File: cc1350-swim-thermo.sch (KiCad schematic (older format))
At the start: 54 parts, among them P1 LMT_70_1, P2 LMT_70_2, P3 SMA FEMALE, P4 USB_OTG, P5 CONN_02X05, Q1 2N7002, SW1 SW_Push, U1 2450BM14G0011T, U2 XMSSJE3G0PA-003, U3 CC1350F128RSM, U4 TLV713, U5 TLC5973, U6 MCP16251, U7 LFB18868MBG9E212, Y1 24MHz, Y2 32.768kHz

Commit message: checked first iteration of pcb with real components
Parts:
- AE1: footprint cc1350:2450AT42A100 -> cc1350:2450AT45A100
- D1: value CLV1A-FKB -> ASMB-MTB0-0A3A2; footprint LEDs:LED_WS2812B-PLCC4 -> cc1350:ASMB-MTB0-0A3A2
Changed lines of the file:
@@
-$EndComp
-$Comp
-L LED_ARGB D1
-U 1 1 58C766EA
-P 8500 3250
-F 0 "D1" H 8500 3620 50  0000 C CNN
-F 1 "CLV1A-FKB" H 8500 2900 50  0000 C CNN
-F 2 "LEDs:LED_WS2812B-PLCC4" H 8500 3200 50  0001 C CNN
-F 3 "" H 8500 3200 50  0000 C CNN
-	1    8500 3250
-	-1   0    0    1
 $EndComp
 $Comp
@@
 NoConn ~ 7350 5250
 $Comp
-L GND #PWR046
+L GND #PWR045
 U 1 1 58CA0220
 P 7250 5450
-F 0 "#PWR046" H 7250 5200 50  0001 C CNN
+F 0 "#PWR045" H 7250 5200 50  0001 C CNN
 F 1 "GND" H 7250 5300 50  0000 C CNN
 F 2 "" H 7250 5450 50  0000 C CNN
@@
 $EndComp
 $Comp
-L GND #PWR047
+L GND #PWR046
 U 1 1 58CA38E4
 P 8550 6000
-F 0 "#PWR047" H 8550 5750 50  0001 C CNN
+F 0 "#PWR046" H 8550 5750 50  0001 C CNN
 F 1 "GND" H 8550 5850 50  0000 C CNN
 F 2 "" H 8550 6000 50  0000 C CNN
@@
 $EndComp
 $Comp
-L GND #PWR048
+L GND #PWR047
 U 1 1 58CC4391
 P 950 1750
-F 0 "#PWR048" H 950 1500 50  0001 C CNN
+F 0 "#PWR047" H 950 1500 50  0001 C CNN
 F 1 "GND" H 950 1600 50  0000 C CNN
 F 2 "" H 950 1750 50  0000 C CNN
@@
 $EndComp
 $Comp
-L GND #PWR049
+L GND #PWR048
 U 1 1 58CC7C22
 P 1050 1300
-F 0 "#PWR049" H 1050 1050 50  0001 C CNN
+F 0 "#PWR048" H 1050 1050 50  0001 C CNN
 F 1 "GND" H 1050 1150 50  0000 C CNN
 F 2 "" H 1050 1300 50  0000 C CNN
@@
 $EndComp
 $Comp
-L GND #PWR051
+L GND #PWR049
 U 1 1 58CC91C7
 P 2150 1300
-F 0 "#PWR051" H 2150 1050 50  0001 C CNN
+F 0 "#PWR049" H 2150 1050 50  0001 C CNN
 F 1 "GND" H 2150 1150 50  0000 C CNN
 F 2 "" H 2150 1300 50  0000 C CNN
@@
 T_ON_1
 $Comp
-L PWR_FLAG #FLG053
+L PWR_FLAG #FLG050
 U 1 1 58CCF366
 P 7700 1700
-F 0 "#FLG053" H 7700 1795 50  0001 C CNN
+F 0 "#FLG050" H 7700 1795 50  0001 C CNN
 F 1 "PWR_FLAG" H 7700 1880 50  0000 C CNN
 F 2 "" H 7700 1700 50  0000 C CNN
@@
 $EndComp
 $Comp
-L PWR_FLAG #FLG054
+L PWR_FLAG #FLG051
 U 1 1 58CD2351
 P 1900 5550
-F 0 "#FLG054" H 1900 5645 50  0001 C CNN
+F 0 "#FLG051" H 1900 5645 50  0001 C CNN
 F 1 "PWR_FLAG" H 1900 5730 50  0000 C CNN
 F 2 "" H 1900 5550 50  0000 C CNN
@@
 $EndComp
 $Comp
-L PWR_FLAG #FLG055
+L PWR_FLAG #FLG052
 U 1 1 58CD3D84
 P 10500 1950
-F 0 "#FLG055" H 10500 2045 50  0001 C CNN
+F 0 "#FLG052" H 10500 2045 50  0001 C CNN
 F 1 "PWR_FLAG" H 10500 2130 50  0000 C CNN
 F 2 "" H 10500 1950 50  0000 C CNN
@@
 	3200 3050 3200 3150
 $Comp
-L PWR_FLAG #FLG056
+L PWR_FLAG #FLG053
 U 1 1 58CD8AB4
 P 2050 4500
-F 0 "#FLG056" H 2050 4595 50  0001 C CNN
+F 0 "#FLG053" H 2050 4595 50  0001 C CNN
 F 1 "PWR_FLAG" H 2050 4680 50  0000 C CNN
 F 2 "" H 2050 4500 50  0000 C CNN
@@
 F 0 "AE1" H 2775 6725 50  0000 R CNN
 F 1 "Antenna" H 2775 6650 50  0000 R CNN
-F 2 "cc1350:2450AT42A100" H 2850 6650 50  0001 C CNN
+F 2 "cc1350:2450AT45A100" H 2850 6650 50  0001 C CNN
 F 3 "" H 2850 6650 50  0001 C CNN
 	1    2850 6650
@@
 	4450 7400 5000 7400
 $Comp
-L GND #PWR057
+L GND #PWR054
 U 1 1 58D43397
 P 5000 7400
-F 0 "#PWR057" H 5000 7150 50  0001 C CNN
+F 0 "#PWR054" H 5000 7150 50  0001 C CNN
 F 1 "GND" H 5000 7250 50  0000 C CNN
 F 2 "" H 5000 7400 50  0000 C CNN
@@
 Connection ~ 4600 7400
 $Comp
-L GND #PWR058
+L GND #PWR055
 U 1 1 58D43708
 P 4950 5800
-F 0 "#PWR058" H 4950 5550 50  0001 C CNN
+F 0 "#PWR055" H 4950 5550 50  0001 C CNN
 F 1 "GND" H 4950 5650 50  0000 C CNN
 F 2 "" H 4950 5800 50  0000 C CNN
@@
 	4800 6700 5000 6700
 $Comp
-L GND #PWR?
+L GND #PWR056
 U 1 1 58D96477
 P 3350 7550
-F 0 "#PWR?" H 3350 7300 50  0001 C CNN
+F 0 "#PWR056" H 3350 7300 50  0001 C CNN
 F 1 "GND" H 3350 7400 50  0000 C CNN
 F 2 "" H 3350 7550 50  0000 C CNN
@@
 Text Label 1950 1300 2    60   ~ 0
 VDDS
+$Comp
+L LED_ARGB D1
+U 1 1 58C766EA
+P 8500 3250
+F 0 "D1" H 8500 3620 50  0000 C CNN
+F 1 "ASMB-MTB0-0A3A2" H 8500 2900 50  0000 C CNN
+F 2 "cc1350:ASMB-MTB0-0A3A2" H 8500 3200 50  0001 C CNN
+F 3 "" H 8500 3200 50  0000 C CNN
+	1    8500 3250
+	-1   0    0    1
+$EndComp
 $EndSCHEMATC

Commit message: Changed r4 value for TLC5973 current limiting experimentally
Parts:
- R4: value 2.08K -> 1.5K
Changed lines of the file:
@@
 P 10100 3250
 F 0 "R4" V 10180 3250 50  0000 C CNN
-F 1 "2.08K" V 10000 3450 50  0000 C CNN
+F 1 "1.5K" V 10000 3450 50  0000 C CNN
 F 2 "Resistors_SMD:R_0603" V 10030 3250 50  0001 C CNN
 F 3 "" H 10100 3250 50  0000 C CNN

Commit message: PCB v1.1
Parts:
- P3: footprint cc1350:sma_female_top -> cc1350:SMA_EdgeMount_Horizontal
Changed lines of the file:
@@
 F 0 "P3" H 5560 6820 50  0000 C CNN
 F 1 "SMA FEMALE" V 5660 6640 50  0000 C CNN
-F 2 "cc1350:sma_female_top" H 5550 6700 50  0001 C CNN
+F 2 "cc1350:SMA_EdgeMount_Horizontal" H 5550 6700 50  0001 C CNN
 F 3 "" H 5550 6700 50  0000 C CNN
 	1    5550 6700

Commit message: Schema for discrete baluns and new switch
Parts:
- removed U1: 2450BM14G0011T, cc1350:2450BM14G011T, symbol 2450BM14G0011T
- removed U2: XMSSJE3G0PA-003, cc1350:XMSSJE3G0PA-003, symbol XMSSJE3G0PA-003
- removed U7: LFB18868MBG9E212, cc1350:LFB18868MBG9E212, symbol LFB18868MBG9E212
- added C10, C14, C28, C29, C7: 3.6pF, symbol C
- added C12, C19, C32: 1pF, symbol C
- added C27, C34: DNM, symbol C
- added C30: 5.6pF, symbol C
- added C31: 3.3pF, symbol C
- added C33, C35: 100pF, symbol C
- added L11, L13, L5: 6.8nH, symbol L
- added L12: 1.5nH, symbol L
- added L14: 7.5nH, symbol L
- added L15, L4, L8: 2.2nH, symbol L
- added L16, L3: DNM, symbol L
- added P6: U.FL, symbol BNC
- added U1: SKY13421-486LF, symbol SKY13421-486LF
- AE1: footprint cc1350:2450AT45A100 -> (none)
- C20: value 100pF -> 3.6pF; footprint Capacitors_SMD:C_0402 -> (none)
- P3: value SMA FEMALE -> SMA; footprint cc1350:SMA_EdgeMount_Horizontal -> (none)
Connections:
- net DIO0_RF_SW_PWR: now also U1.7 (VDD)
- net DIO1_RF_SW: now also U1.12 (VCTL)
- net GND: now also C10.2, C12.2, C14.1, C27.2, C28.2, C29.2, C30.2, C31.2, C32.2, C7.1, L16.2, L4.1, L5.2, P6.2 (Ext), U1.0 (PAD), U1.1 (GND), U1.11 (GND), U1.13 (GND), U1.4 (GND), U1.6 (GND), U1.8 (GND)
- net RF_N_BIAS: now reaches C5.1
- net RF_N_BIAS: now also U1.10 (RFCA)
- net RF_P_BIAS: now reaches C4.1
- net RF_P_BIAS: now also U1.9 (RFCB)
- net at AE1.1 (A): now also C35.1, L16.1
- net at C20.1: now also C28.1, L11.2, L13.1; no longer P3.1 (In)
- net at C20.2: now also C10.1, L5.1, U1.2 (RF1B)
- new net: C14.2, C7.2, L11.1, U1.14 (RF1A)
- new net: C19.2, L3.1, L4.2, U1.3 (RF2A)
- new net: C12.1, L3.2, L8.2, U1.5 (RF2B)
- new net: C30.1, L13.2, L14.1
- new net: C31.1, C33.2, L14.2
- new net: C33.1, P3.1 (In)
- new net: C19.1, C27.1, L12.1, L8.1
- new net: C29.1, L12.2, L15.1
- new net: C32.1, C34.2, C35.2, L15.2
- new net: C34.1, P6.1 (In)
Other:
- note added: "2.4 GHz balun and antenna"
- note added: "868 MHz balun and antenna"
- note added: "Antenna matching"
- note removed: "868MHz RF section"
- note removed: "BLE RF section"
- moved on the sheet: C18, L6, L7

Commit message: Updated schema to kicad v5 and new footprints
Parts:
- removed D1: ASMB-MTB0-0A3A2, cc1350:ASMB-MTB0-0A3A2, symbol LED_ARGB
- removed P1: LMT_70_1, Connectors_Molex:Molex_KK-6410-04_04x2.54mm_Straight, symbol CONN_01X04
- removed P2: LMT_70_2, Connectors_Molex:Molex_KK-6410-04_04x2.54mm_Straight, symbol CONN_01X04
- removed P3: SMA, symbol BNC
- removed P4: USB_OTG, Connectors:USB_Mini-B, symbol USB_OTG
- removed P5: CONN_02X05, cc1350:Pin_Header_Straight_SMT_02x05_1_27mm, symbol CONN_02X05
- removed P6: U.FL, symbol BNC
- removed SW1: SW_Push, cc1350:SKSLLAE010, symbol SW_Push
- added D1: ASMB-MTB0-0A3A2, cc1350:ASMB-MTB0-0A3A2, symbol Device:LED_ARGB
- added J1: LMT_70_1, Connector_Molex:Molex_KK-254_AE-6410-04A_1x04_P2.54mm_Vertical, symbol Connector_Generic:Conn_01x04
- added J2: LMT_70_2, Connector_Molex:Molex_KK-254_AE-6410-04A_1x04_P2.54mm_Vertical, symbol Connector_Generic:Conn_01x04
- added J3: SMA, Connector_Coaxial:SMA_Amphenol_132289_EdgeMount, symbol Connector:Conn_Coaxial
- added J4: U.FL, cc1350:U.FL_Hirose_U.FL-R-SMT-1_Vertical, symbol Connector:Conn_Coaxial
- added J5: USB_B_Micro, Connector_USB:USB_Mini-B_Lumberg_2486_01_Horizontal, symbol Connector:USB_B_Micro
- added J6: Conn_02x05_Odd_Even, cc1350:Pin_Header_Straight_SMT_02x05_1_27mm, symbol Connector_Generic:Conn_02x05_Odd_Even
- added SW1: SW_Push, cc1350:SKSLLAE010, symbol Switch:SW_Push
- AE1: footprint (none) -> cc1350:2450AT45A100; symbol Antenna -> Device:Antenna
- BT1: symbol Battery -> Device:Battery
- C1, C13, C15, C16, C17, C18, C2, C21, C22, C23, C24, C25, C26, C3, C6: footprint Capacitors_SMD:C_0603 -> Capacitor_SMD:C_0603_1608Metric; symbol C -> Device:C
- C10, C12, C14, C19, C20, C28, C29, C30, C31, C32, C33, C35, C7: footprint (none) -> Capacitor_SMD:C_0402_1005Metric; symbol C -> Device:C
- C11: footprint Capacitors_SMD:C_0603 -> Capacitor_SMD:C_0402_1005Metric; symbol C -> Device:C
- C27, C34: symbol C -> Device:C
- C4, C5, C8, C9: footprint Capacitors_SMD:C_0402 -> Capacitor_SMD:C_0402_1005Metric; symbol C -> Device:C
- JP1: symbol Jumper_NC_Small -> Device:Jumper_NC_Small
- L1, L2: footprint Resistors_SMD:R_0402 -> Inductor_SMD:L_0402_1005Metric; symbol L -> Device:L
- L10, L16, L3: symbol L -> Device:L
- L11, L12, L13, L14, L15, L4, L5, L8: footprint (none) -> Inductor_SMD:L_0402_1005Metric; symbol L -> Device:L
- L6, L9: footprint Resistors_SMD:R_0603 -> Inductor_SMD:L_0603_1608Metric; symbol Ferrite_Bead -> Device:Ferrite_Bead
- L7: footprint Resistors_SMD:R_0805 -> Inductor_SMD:L_0805_2012Metric; symbol L -> Device:L
- Q1: symbol Q_NMOS_GSD -> Device:Q_NMOS_GSD
- R1, R2, R3, R4, R5, R6, R7: footprint Resistors_SMD:R_0603 -> Resistor_SMD:R_0603_1608Metric; symbol R -> Device:R
- U1: footprint (none) -> cc1350:SKY13421-486LF; symbol SKY13421-486LF -> cc1350:SKY13421-486LF
- U3: symbol CC1350F128RSM -> cc1350:CC1350F128RSM
- U4: symbol TLV713 -> cc1350:TLV713
- U5: symbol TLC5973 -> cc1350:TLC5973
- U6: symbol MCP16251 -> cc1350:MCP16251
- Y1: symbol Crystal_GND24 -> Device:Crystal_GND24
- Y2: symbol Crystal -> Device:Crystal
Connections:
- wire segments 218 -> 276

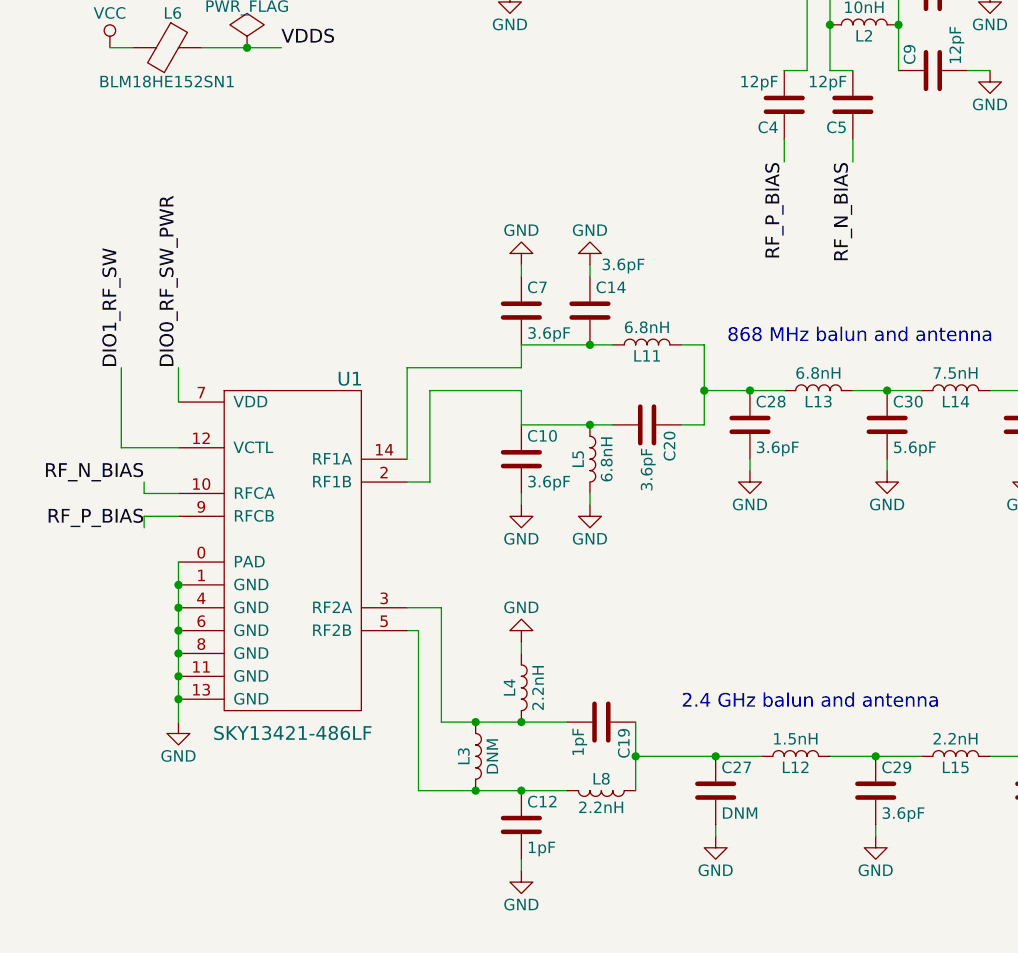
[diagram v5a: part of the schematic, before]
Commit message: PCB v1.2 ready for manufacturing
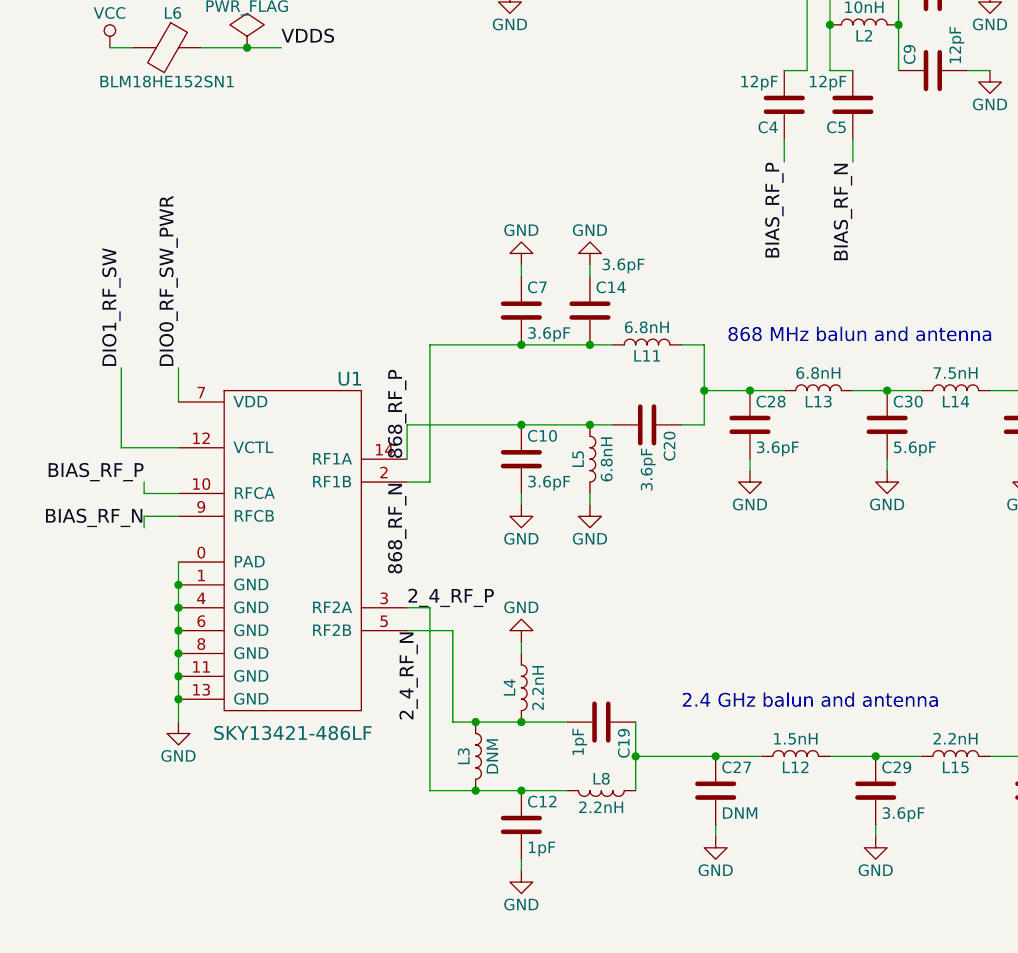
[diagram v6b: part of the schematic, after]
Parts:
- C27, C34: footprint (none) -> Capacitor_SMD:C_0402_1005Metric
- L16, L3: footprint (none) -> Inductor_SMD:L_0402_1005Metric
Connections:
- net labels added: 2_4_RF_N, 2_4_RF_P, 868_RF_N, 868_RF_P, BIAS_RF_N, BIAS_RF_P
- net labels removed: RF_N_BIAS, RF_P_BIAS
- wire segments 276 -> 274
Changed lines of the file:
@@
 VDDS
 Text Label 3750 4500 3    60   ~ 0
-RF_P_BIAS
+BIAS_RF_P
 Text Label 4050 4500 3    60   ~ 0
-RF_N_BIAS
+BIAS_RF_N
 Wire Wire Line
 	4050 4400 4050 4500
 Wire Wire Line
 	3750 4400 3750 4500
-Text Label 950  5900 2    60   ~ 0
-RF_N_BIAS
+Text Label 950  6100 2    60   ~ 0
+BIAS_RF_N
 $Comp
 L cc1350:SKY13421-486LF U1
@@
 Wire Wire Line
 	950  5950 950  5900
-Text Label 950  6100 2    60   ~ 0
-RF_P_BIAS
+Text Label 950  5900 2    60   ~ 0
+BIAS_RF_P
 Wire Wire Line
 	1100 6050 950  6050
 Wire Wire Line
 	950  6050 950  6100
-Wire Wire Line
-	1100 6250 1100 6350
-Connection ~ 1100 6350
-Connection ~ 1100 6450
-Connection ~ 1100 6550
-Connection ~ 1100 6650
-Connection ~ 1100 6750
-Connection ~ 1100 6850
 $Comp
 L power:GND #PWR051
@@
 F 0 "C34" H 5425 6350 50  0000 L CNN
 F 1 "DNM" H 5425 6150 50  0000 L CNN
-F 2 "" H 5438 6100 50  0001 C CNN
+F 2 "Capacitor_SMD:C_0402_1005Metric" H 5438 6100 50  0001 C CNN
 F 3 "" H 5400 6250 50  0000 C CNN
 	1    5400 6250
@@
 F 0 "L16" V 5800 7250 50  0000 C CNN
 F 1 "DNM" V 5925 7250 50  0000 C CNN
-F 2 "" H 5850 7250 50  0001 C CNN
+F 2 "Inductor_SMD:L_0402_1005Metric" H 5850 7250 50  0001 C CNN
 F 3 "" H 5850 7250 50  0000 C CNN
 	1    5850 7250
@@
 	2100 5900 2200 5900
 Wire Wire Line
-	2200 5900 2200 5500
-Wire Wire Line
-	2200 5500 2600 5500
-Wire Wire Line
-	2600 5300 2600 5400
-Wire Wire Line
-	2600 5400 2100 5400
-Wire Wire Line
-	2100 5400 2100 5800
-Wire Wire Line
-	2600 5500 2600 5650
-Wire Wire Line
 	2600 5300 2900 5300
 Connection ~ 2900 5300
@@
 Wire Wire Line
 	6000 5700 6000 5750
-Wire Wire Line
-	2250 6950 2400 6950
 Connection ~ 2600 6950
-Wire Wire Line
-	2150 7250 2400 7250
 Wire Wire Line
 	2600 7550 2600 7600
@@
 Wire Wire Line
 	2600 6600 2600 6650
-Wire Wire Line
-	2250 6950 2250 6450
-Wire Wire Line
-	2250 6450 2100 6450
-Wire Wire Line
-	2100 6550 2150 6550
-Wire Wire Line
-	2150 6550 2150 7250
 Wire Wire Line
 	3950 7100 4150 7100
@@
 F 0 "C27" H 3475 7350 50  0000 L CNN
 F 1 "DNM" H 3475 7150 50  0000 L CNN
-F 2 "" H 3488 7100 50  0001 C CNN
+F 2 "Capacitor_SMD:C_0402_1005Metric" H 3488 7100 50  0001 C CNN
 F 3 "" H 3450 7250 50  0000 C CNN
 	1    3450 7250
@@
 $EndComp
 Connection ~ 2400 7250
-Connection ~ 2400 6950
 $Comp
 L Device:L L3
@@
 F 0 "L3" V 2350 7100 50  0000 C CNN
 F 1 "DNM" V 2475 7100 50  0000 C CNN
-F 2 "" H 2400 7100 50  0001 C CNN
+F 2 "Inductor_SMD:L_0402_1005Metric" H 2400 7100 50  0001 C CNN
 F 3 "" H 2400 7100 50  0000 C CNN
 	1    2400 7100
@@
 Wire Wire Line
 	1550 2950 1700 2950
-Wire Wire Line
-	1100 6350 1100 6450
-Wire Wire Line
-	1100 6450 1100 6550
-Wire Wire Line
-	1100 6550 1100 6650
-Wire Wire Line
-	1100 6650 1100 6750
-Wire Wire Line
-	1100 6750 1100 6850
-Wire Wire Line
-	1100 6850 1100 6950
 Wire Wire Line
 	2900 5300 3000 5300
@@
 Wire Wire Line
 	6700 2450 6600 2450
+Wire Wire Line
+	2600 5650 2100 5650
+Wire Wire Line
+	2100 5650 2100 5800
+Connection ~ 2600 5650
+Wire Wire Line
+	2200 5300 2600 5300
+Wire Wire Line
+	2200 5300 2200 5900
+Connection ~ 2600 5300
+Wire Wire Line
+	2100 6550 2300 6550
+Wire Wire Line
+	2100 6450 2200 6450
+Wire Wire Line
+	2200 6450 2200 7250
+Wire Wire Line
+	2200 7250 2400 7250
+Wire Wire Line
+	2300 6550 2300 6950
+Wire Wire Line
+	2300 6950 2400 6950
+Connection ~ 2400 6950
+Text Label 2100 5800 1    60   ~ 0
+868_RF_P
+Wire Wire Line
+	1100 6850 1100 6950
+Wire Wire Line
+	1100 6750 1100 6850
+Wire Wire Line
+	1100 6650 1100 6750
+Wire Wire Line
+	1100 6550 1100 6650
+Wire Wire Line
+	1100 6450 1100 6550
+Connection ~ 1100 6850
+Connection ~ 1100 6750
+Connection ~ 1100 6650
+Connection ~ 1100 6550
+Connection ~ 1100 6450
+Connection ~ 1100 6350
+Wire Wire Line
+	1100 6350 1100 6450
+Wire Wire Line
+	1100 6250 1100 6350
+Text Label 2100 5900 3    60   ~ 0
+868_RF_N
+Text Label 2100 6450 0    60   ~ 0
+2_4_RF_P
+Text Label 2150 6550 3    60   ~ 0
+2_4_RF_N
 $EndSCHEMATC

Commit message: PCB sent to manufacturing
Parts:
- added L17: DNM, Inductor_SMD:L_0402_1005Metric, symbol Device:L
- BT1: footprint cc1350:2_AAA_batteryholder_keystone -> Connector_Molex:Molex_KK-254_AE-6410-02A_1x02_P2.54mm_Vertical
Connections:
- wire segments 274 -> 276
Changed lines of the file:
@@
 F 0 "BT1" H 10600 1800 50  0000 L CNN
 F 1 "Battery" H 10600 1700 50  0000 L CNN
-F 2 "cc1350:2_AAA_batteryholder_keystone" V 10500 1760 50  0001 C CNN
+F 2 "Connector_Molex:Molex_KK-254_AE-6410-02A_1x02_P2.54mm_Vertical" V 10500 1760 50  0001 C CNN
 F 3 "" V 10500 1760 50  0000 C CNN
 	1    10500 1700
@@
 	3600 5800 3600 5850
 Wire Wire Line
-	5550 5500 5800 5500
+	5550 5500 5700 5500
 Wire Wire Line
 	6000 5700 6000 5750
@@
 Text Label 2150 6550 3    60   ~ 0
 2_4_RF_N
+$Comp
+L Device:L L17
+U 1 1 5B80616F
+P 5700 5650
+F 0 "L17" V 5650 5650 50  0000 C CNN
+F 1 "DNM" V 5775 5650 50  0000 C CNN
+F 2 "Inductor_SMD:L_0402_1005Metric" H 5700 5650 50  0001 C CNN
+F 3 "" H 5700 5650 50  0000 C CNN
+	1    5700 5650
+	1    0    0    -1
+$EndComp
+Connection ~ 5700 5500
+Wire Wire Line
+	5700 5500 5800 5500
+$Comp
+L power:GND #PWR0102
+U 1 1 5B806283
+P 5700 5850
+F 0 "#PWR0102" H 5700 5600 50  0001 C CNN
+F 1 "GND" H 5700 5700 50  0000 C CNN
+F 2 "" H 5700 5850 50  0000 C CNN
+F 3 "" H 5700 5850 50  0000 C CNN
+	1    5700 5850
+	1    0    0    -1
+$EndComp
+Wire Wire Line
+	5700 5800 5700 5850
 $EndSCHEMATC

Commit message: pcb revision v1.3 after tests
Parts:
- C11: footprint Capacitor_SMD:C_0402_1005Metric -> Capacitor_SMD:C_0603_1608Metric
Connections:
- wire segments 276 -> 277
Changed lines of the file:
@@
 F 0 "C11" V 4650 650 50  0000 L CNN
 F 1 "100nF" V 4650 900 50  0000 L CNN
-F 2 "Capacitor_SMD:C_0402_1005Metric" H 4638 700 50  0001 C CNN
+F 2 "Capacitor_SMD:C_0603_1608Metric" H 4638 700 50  0001 C CNN
 F 3 "" H 4600 850 50  0000 C CNN
 	1    4600 850
@@
 Text Label 4150 1200 2    60   ~ 0
 RESET_N
-Text Label 8550 4900 0    60   ~ 0
-VDDS
 $Comp
 L Device:R R3
@@
 Text Label 1550 4000 0    60   ~ 0
 VDDS
-Text Label 7150 4950 2    60   ~ 0
-VDDS
-Text Label 850  1300 2    60   ~ 0
-VDDS
-Text Label 1950 1300 2    60   ~ 0
-VDDS
 Text Label 3750 4500 3    60   ~ 0
 BIAS_RF_P
@@
 $EndComp
 Wire Wire Line
-	7150 4950 7350 4950
-Wire Wire Line
 	7150 5050 7350 5050
 Wire Wire Line
@@
 Wire Wire Line
 	5700 5800 5700 5850
+$Comp
+L power:VCC #PWR?
+U 1 1 5B94A0C0
+P 850 1300
+F 0 "#PWR?" H 850 1150 50  0001 C CNN
+F 1 "VCC" H 867 1473 50  0000 C CNN
+F 2 "" H 850 1300 50  0001 C CNN
+F 3 "" H 850 1300 50  0001 C CNN
+	1    850  1300
+	1    0    0    -1
+$EndComp
+$Comp
+L power:VCC #PWR?
+U 1 1 5B94A1D3
+P 1950 1300
+F 0 "#PWR?" H 1950 1150 50  0001 C CNN
+F 1 "VCC" H 1967 1473 50  0000 C CNN
+F 2 "" H 1950 1300 50  0001 C CNN
+F 3 "" H 1950 1300 50  0001 C CNN
+	1    1950 1300
+	1    0    0    -1
+$EndComp
+$Comp
+L power:VCC #PWR?
+U 1 1 5B98BF41
+P 7000 4950
+F 0 "#PWR?" H 7000 4800 50  0001 C CNN
+F 1 "VCC" H 7017 5123 50  0000 C CNN
+F 2 "" H 7000 4950 50  0001 C CNN
+F 3 "" H 7000 4950 50  0001 C CNN
+	1    7000 4950
+	1    0    0    -1
+$EndComp
+$Comp
+L power:VCC #PWR?
+U 1 1 5B98C054
+P 8900 4900
+F 0 "#PWR?" H 8900 4750 50  0001 C CNN
+F 1 "VCC" H 8917 5073 50  0000 C CNN
+F 2 "" H 8900 4900 50  0001 C CNN
+F 3 "" H 8900 4900 50  0001 C CNN
+	1    8900 4900
+	1    0    0    -1
+$EndComp
+Wire Wire Line
+	8550 4900 8900 4900
+Wire Wire Line
+	7000 4950 7350 4950
 $EndSCHEMATC
